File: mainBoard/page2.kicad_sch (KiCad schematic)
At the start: 31 parts, among them IC1 TCAN3414DR, J10 RJ45, J11 RJ45, J12 Conn_01x03, J13 RJ45, J14 RJ45, J15 RJ45, J16 BM04B-SRSS-TB, J17 BM04B-SRSS-TB, J18 BM04B-SRSS-TB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

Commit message: removed 3 of the can ports, re-layed out the buck converters, exported new step
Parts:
- removed J13, J14, J15: RJ45, Connector_RJ:RJ45_OST_PJ012-8P8CX_Vertical, symbol Connector:RJ45
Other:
- moved on the sheet: J10, J11, J7, J8, J9

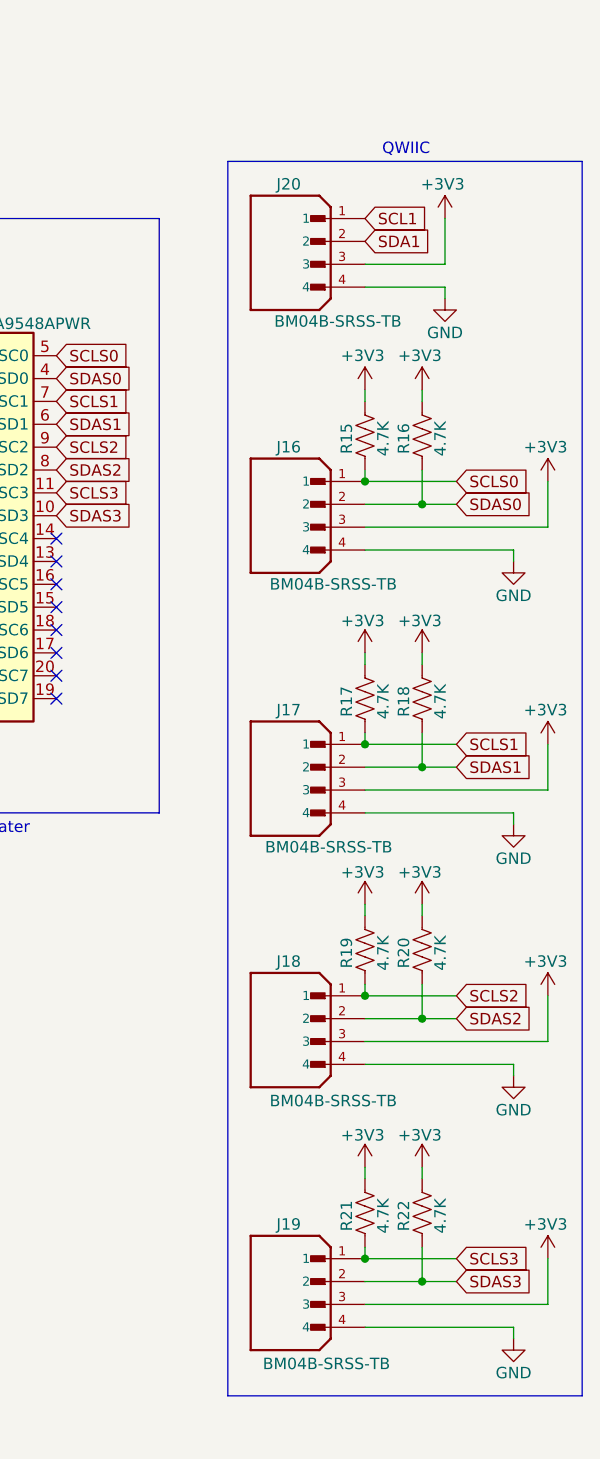
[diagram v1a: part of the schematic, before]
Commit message: Reviewed PCB with justin and made changes
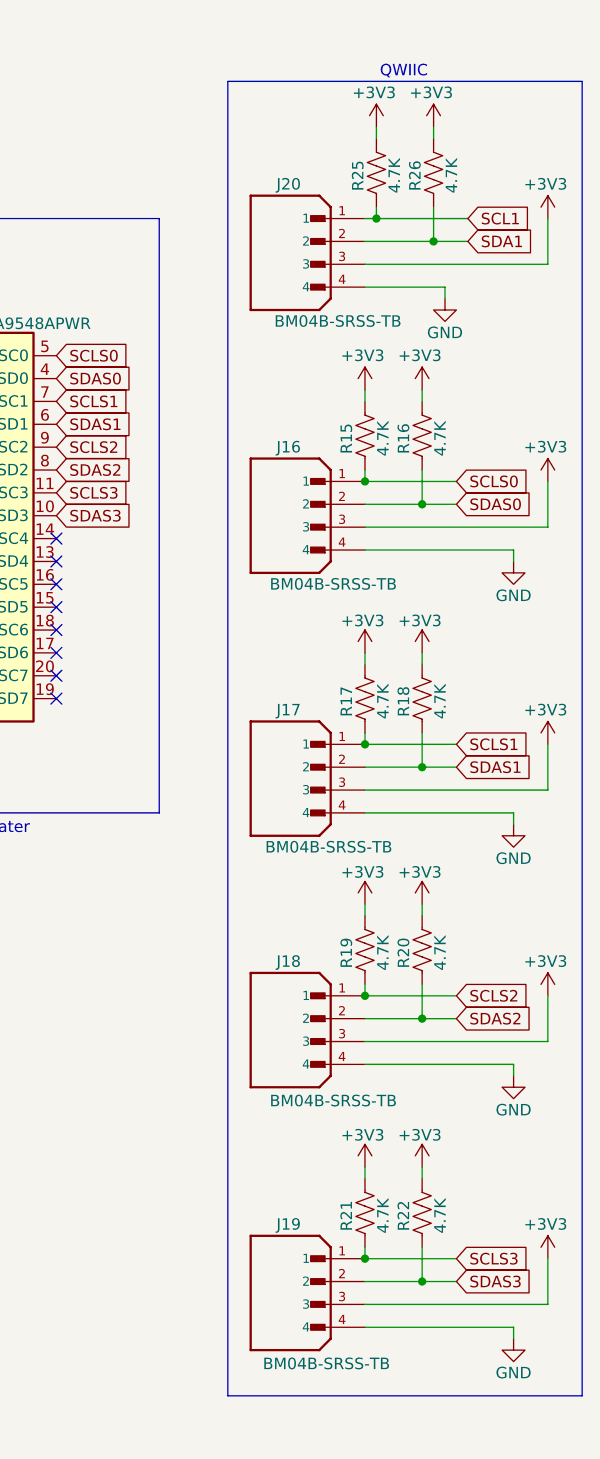
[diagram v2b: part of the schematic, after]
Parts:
- added R25, R26: 4.7K, Resistor_SMD:R_0805_2012Metric_Pad1.20x1.40mm_HandSolder, symbol Device:R_US
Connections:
- net +3V3: now also R25.1, R26.1
- net SCL1: now also R25.2
- net SDA1: now also R26.2
